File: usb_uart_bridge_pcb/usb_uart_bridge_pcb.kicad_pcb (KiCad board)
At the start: 2 copper layers, 20 x 16 mm, 23 parts

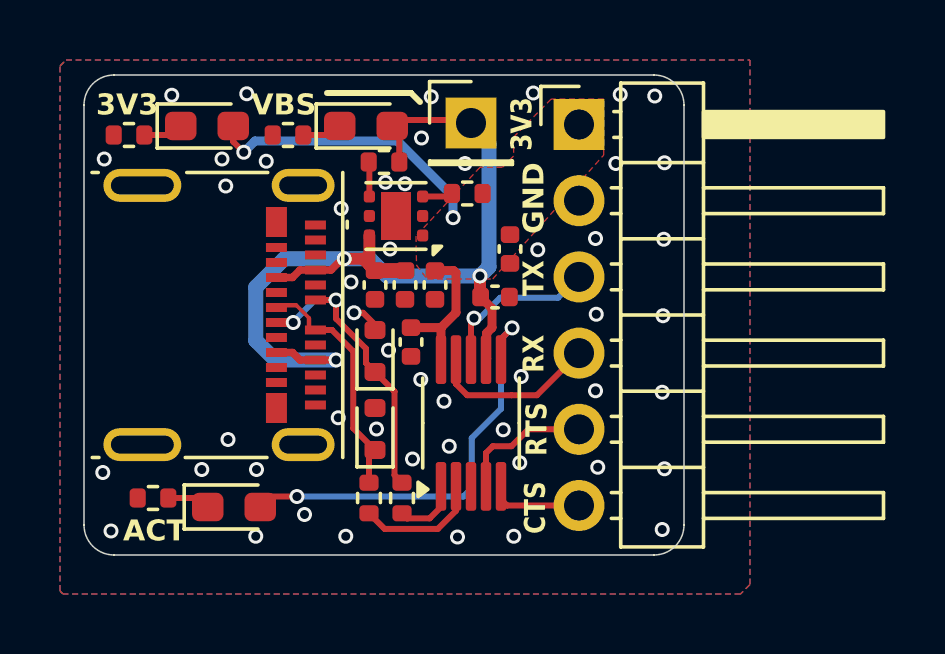
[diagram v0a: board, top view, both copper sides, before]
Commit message: 1. fixed missing 5.1K resistors
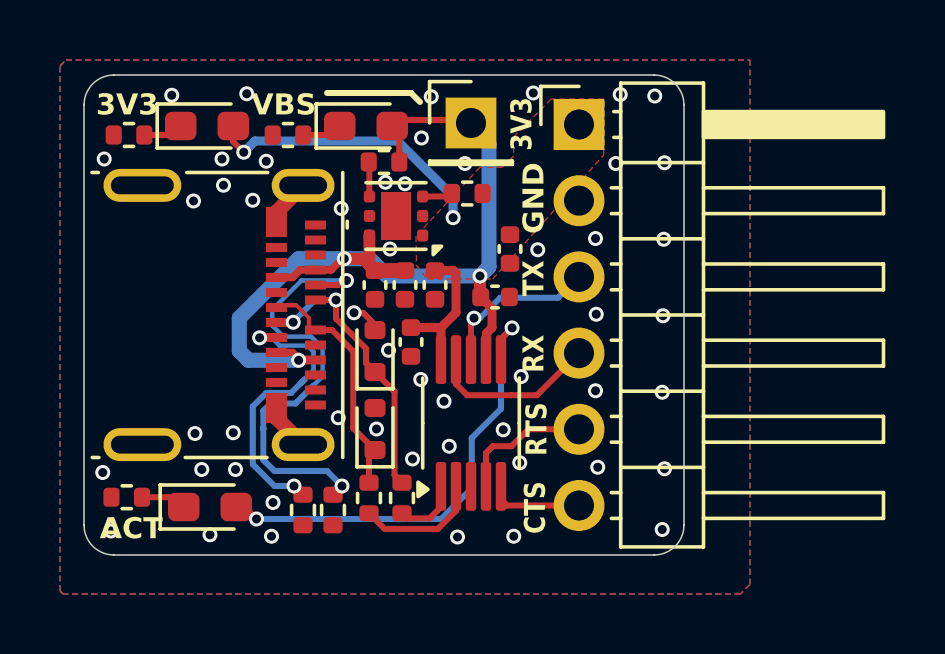
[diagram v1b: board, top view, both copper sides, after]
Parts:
- added R8: 5.1k, Resistor_SMD:R_0402_1005Metric, F.Cu at (126.8, 74.5)
- added R9: 5.1k, Resistor_SMD:R_0402_1005Metric, F.Cu at (125.8, 74.5)
- R3, R4, R5, R6, R7: value 4.7k -> 5.1k
- moved R3 0.88 mm to (119.9, 74.1)
- moved D3 0.80 mm to (122.7, 74.4)
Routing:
- net /NET-(J1-A5): track 0.00 -> 14.7 mm, vias 0 -> 2
- net /NET-(J1-B5): track 0.00 -> 9.90 mm, vias 0 -> 2
- net /GND: track 1.04 -> 4.22 mm, vias 50 -> 52
- net /TNOW: track 14.4 -> 15.6 mm
- net /VBUS: track 33.8 -> 33.1 mm
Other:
- board text added: "USB-UART BRIDGE V1"
- board text removed: "USB- UART BRGE V1"
